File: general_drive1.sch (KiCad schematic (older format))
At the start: 9 parts, among them P22 CONN_1, P23 CONN_1, Q8 PIP-3104

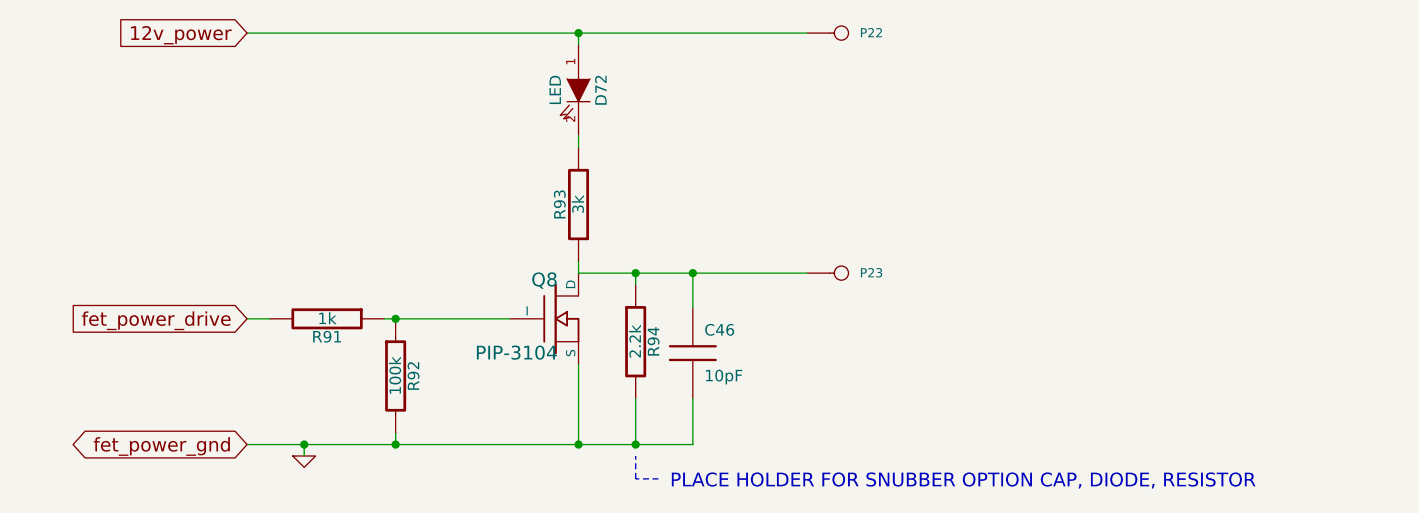
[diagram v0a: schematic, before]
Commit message: DFH mans up a bit. Perhaps usable for something at this point, like making trips to the local store ;)
I connected TA pins to sub circuits, fixed a number if items discussed in the DIYEFI forums. This is it's 21st version, so it was time for it to man up a bit, and become something potentially useful.

Signed-off-by: Jared Harvey <TortiseGIT@jaredharvey.com>
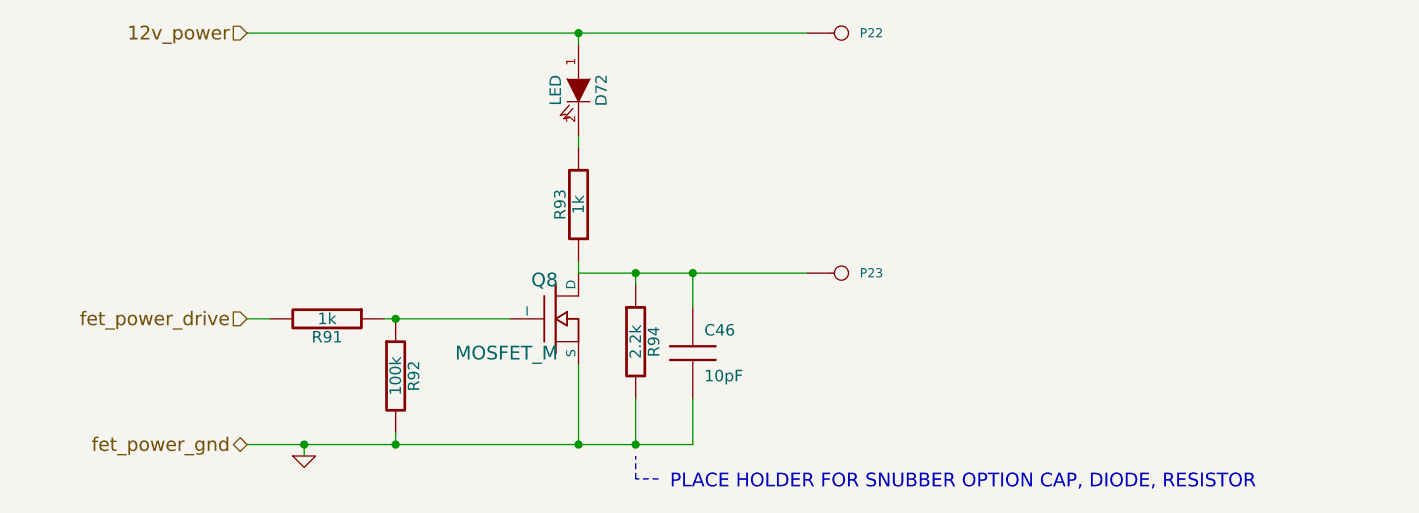
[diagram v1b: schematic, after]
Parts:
- C46: Field10 (none) -> multilayer ceramic; Field11 (none) -> other,more,stuff; Field4 (none) -> newark,97k4148; Field5 (none) -> vendor1, smd w hem; Field6 (none) -> vendor2, thru w hem; Field7 (none) -> vendor2, smd w hem; Field8 (none) -> 200,V; Field9 (none) -> 10,%
- D72: A (none) -> 10mA; V (none) -> 12V; construct (none) -> LED with resistor included; misc (none) -> other,more,stuff; vend1,smd e hem (none) -> newark,; vend2, smd w hem (none) -> digi,; vend2, thru w hem (none) -> digi,; vendor1, thru e hem (none) -> newark,58K2517
- Q8: value PIP-3104 -> MOSFET_M; A (none) -> 28A; V (none) -> 42V; construct (none) -> OVP protected MOSFET; misc (none) -> other,more,stuff; vend1,smd e hem (none) -> newark,; vend2, smd w hem (none) -> digi,; vend2, thru w hem (none) -> digi,VNP28N04-E-ND; vendor1, thru e hem (none) -> element14,1739427
- R91: W (none) -> 1/4w; construct (none) -> carbon film; misc (none) -> other,more,stuff; tol (none) -> 5%; vend1,smd e hem (none) -> newark,52K9725; vend2, smd w hem (none) -> digi,CRCW08051K00JNEA; vend2, thru w hem (none) -> digi,OD102J-ND; vendor1, thru e hem (none) -> newark,65K2365
- R92: Field10 (none) -> carbon film; Field11 (none) -> other,more,stuff; Field4 (none) -> newark,38k0329; Field5 (none) -> vendor1, smd w hem; Field6 (none) -> vendor2, thru w hem; Field7 (none) -> vendor2, smd w hem; Field8 (none) -> 250,mW; Field9 (none) -> 5,%
- R93: value 3k -> 1k; W (none) -> 1/4w; construct (none) -> carbon film; misc (none) -> other,more,stuff; tol (none) -> 5%; vend1,smd e hem (none) -> newark,52K9725; vend2, smd w hem (none) -> digi,CRCW08051K00JNEA; vend2, thru w hem (none) -> digi,OD102J-ND; vendor1, thru e hem (none) -> newark,65K2365
- R94: Field10 (none) -> carbon film; Field11 (none) -> other,more,stuff; Field4 (none) -> newark,38k0352; Field5 (none) -> vendor1, smd w hem; Field6 (none) -> vendor2, thru w hem; Field7 (none) -> vendor2, smd w hem; Field8 (none) -> 250,mW; Field9 (none) -> 5,%
